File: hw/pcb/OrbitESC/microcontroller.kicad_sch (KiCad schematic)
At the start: 82 parts, among them J2 Micro_SD_Card_Det, J6 CAN1, J7 Serial1, J8 Serial2, J9 CAN2, U1 TLE9250X, U10 TLE9250X, U2 AT25SF081-SSHD-X, U3 24LC128, U4 STM32F446ZCHx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

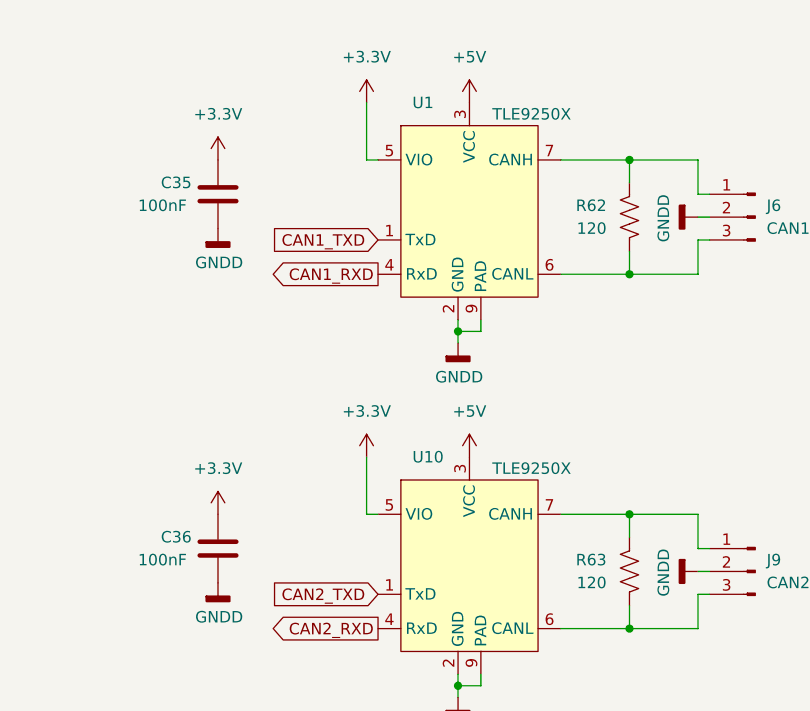
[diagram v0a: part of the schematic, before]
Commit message: Update PCB to match schematic
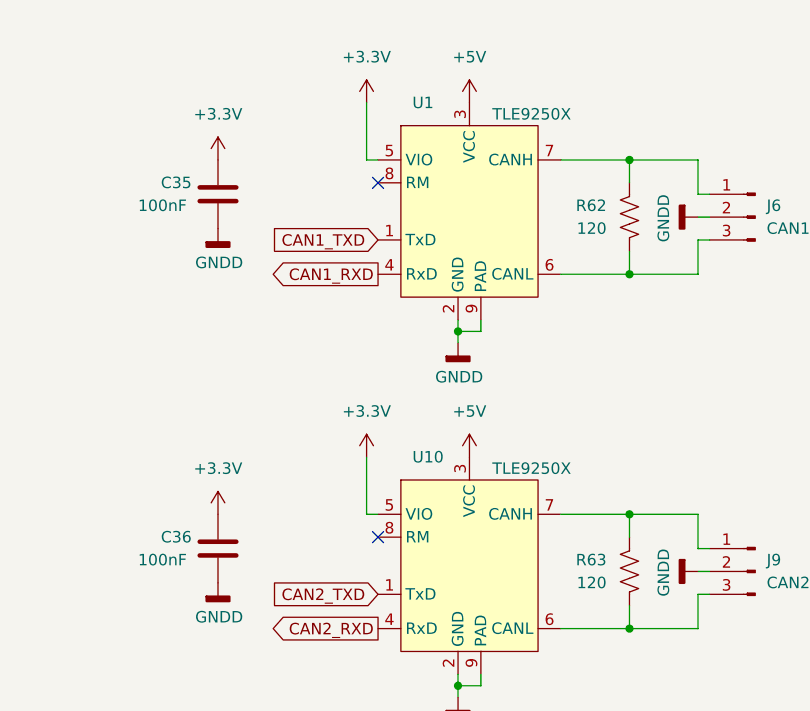
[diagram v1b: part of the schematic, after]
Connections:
- no-connect marks 55 -> 57
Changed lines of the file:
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@@
   (junction (at 212.09 59.69) (diameter 0) (color 0 0 0 0)
   )
+  (no_connect (at 54.61 153.67))
+  (no_connect (at 54.61 193.04))
   (no_connect (at 232.41 124.46))
   (no_connect (at 166.37 114.3))
@@
     (pin "2")
   )
-  (symbol (lib_id "CANTransciever:TLE9250X") (at 64.77 196.85 0) (unit 1)
+  (symbol (lib_name "TLE9250X_1") (lib_id "CANTransciever:TLE9250X") (at 64.77 196.85 0) (unit 1)
     (in_bom yes) (on_board yes)
     (property "Reference" "U10" (id 0) (at 58.42 184.15 0)
@@
     (pin "6")
     (pin "7")
+    (pin "8")
     (pin "9")
   )
@@
       (effects (font (size 1.27 1.27)) hide)
     )
-    (property "Datasheet" "https://www.mouser.com/datasheet/2/590/DS-AT25SF081_045-1385733.pdf" (id 3) (at 337.82 208.28 0)
+    (property "Datasheet" "https://www.adestotech.com/wp-content/uploads/DS-AT25SF081_045.pdf" (id 3) (at 337.82 208.28 0)
       (effects (font (size 1.27 1.27)) hide)
     )
@@
     (pin "6")
     (pin "7")
+    (pin "8")
     (pin "9")
   )

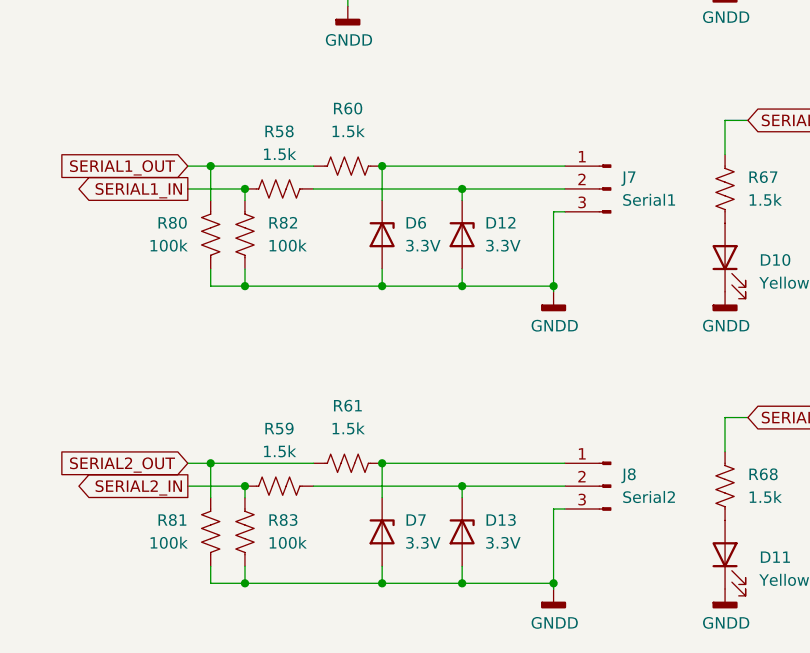
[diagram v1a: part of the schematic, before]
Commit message: Route analogs and power stage sections
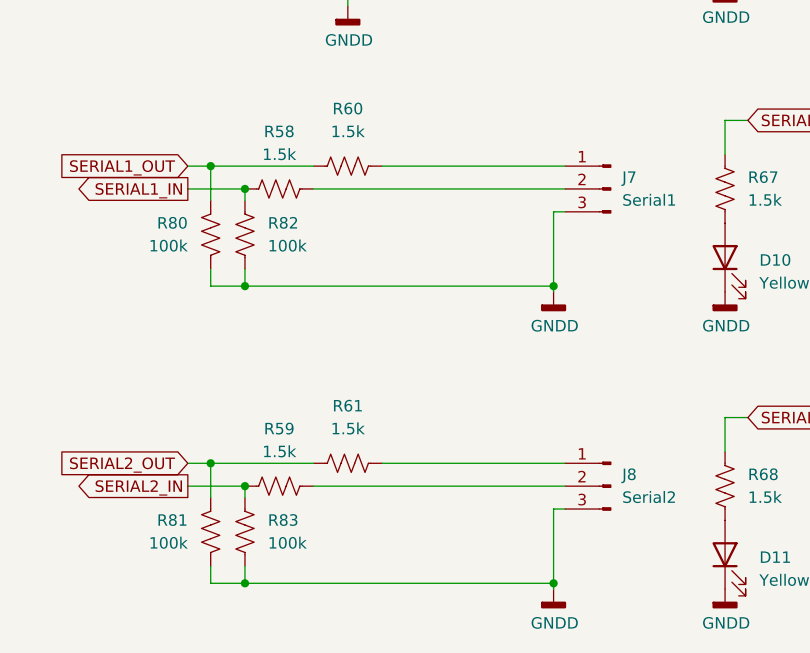
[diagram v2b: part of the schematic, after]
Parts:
- removed D12, D13, D6, D7: 3.3V, Diode_SMD:D_MiniMELF, symbol Device:D_Zener
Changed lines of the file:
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@@
   (junction (at 34.29 27.94) (diameter 0) (color 0 0 0 0)
   )
-  (junction (at 76.2 264.16) (diameter 0) (color 0 0 0 0)
-  )
-  (junction (at 67.31 261.62) (diameter 0) (color 0 0 0 0)
-  )
-  (junction (at 76.2 231.14) (diameter 0) (color 0 0 0 0)
-  )
   (junction (at 196.85 248.92) (diameter 0) (color 0 0 0 0)
   )
@@
   (junction (at 49.53 45.72) (diameter 0) (color 0 0 0 0)
   )
-  (junction (at 67.31 228.6) (diameter 0) (color 0 0 0 0)
-  )
   (junction (at 207.01 59.69) (diameter 0) (color 0 0 0 0)
   )
@@
   (junction (at 304.8 100.33) (diameter 0) (color 0 0 0 0)
   )
-  (junction (at 67.31 241.935) (diameter 0) (color 0 0 0 0)
-  )
   (junction (at 304.8 115.57) (diameter 0) (color 0 0 0 0)
   )
@@
   (junction (at 199.39 248.92) (diameter 0) (color 0 0 0 0)
   )
-  (junction (at 76.2 274.955) (diameter 0) (color 0 0 0 0)
-  )
   (junction (at 82.55 163.83) (diameter 0) (color 0 0 0 0)
   )
@@
   (junction (at 204.47 248.92) (diameter 0) (color 0 0 0 0)
   )
-  (junction (at 76.2 241.935) (diameter 0) (color 0 0 0 0)
-  )
   (junction (at 308.61 210.82) (diameter 0) (color 0 0 0 0)
   )
   (junction (at 321.31 205.74) (diameter 0) (color 0 0 0 0)
   )
-  (junction (at 67.31 274.955) (diameter 0) (color 0 0 0 0)
-  )
   (junction (at 82.55 151.13) (diameter 0) (color 0 0 0 0)
   )
@@
     (stroke (width 0) (type default) (color 0 0 0 0))
   )
-  (wire (pts (xy 76.2 273.05) (xy 76.2 274.955))
-    (stroke (width 0) (type default) (color 0 0 0 0))
-  )
   (wire (pts (xy 322.58 213.36) (xy 308.61 213.36))
     (stroke (width 0) (type default) (color 0 0 0 0))
@@
     (stroke (width 0) (type default) (color 0 0 0 0))
   )
-  (wire (pts (xy 76.2 231.14) (xy 87.63 231.14))
+  (wire (pts (xy 59.69 231.14) (xy 87.63 231.14))
     (stroke (width 0) (type default) (color 0 0 0 0))
   )
@@
     (stroke (width 0) (type default) (color 0 0 0 0))
   )
-  (wire (pts (xy 67.31 240.03) (xy 67.31 241.935))
-    (stroke (width 0) (type default) (color 0 0 0 0))
-  )
   (wire (pts (xy 347.98 175.26) (xy 337.82 175.26))
     (stroke (width 0) (type default) (color 0 0 0 0))
@@
     (stroke (width 0) (type default) (color 0 0 0 0))
   )
-  (wire (pts (xy 76.2 264.16) (xy 87.63 264.16))
-    (stroke (width 0) (type default) (color 0 0 0 0))
-  )
   (wire (pts (xy 204.47 59.69) (xy 204.47 63.5))
     (stroke (width 0) (type default) (color 0 0 0 0))
@@
     (stroke (width 0) (type default) (color 0 0 0 0))
   )
-  (wire (pts (xy 67.31 273.05) (xy 67.31 274.955))
-    (stroke (width 0) (type default) (color 0 0 0 0))
-  )
   (wire (pts (xy 321.31 203.2) (xy 322.58 203.2))
     (stroke (width 0) (type default) (color 0 0 0 0))
@@
     (stroke (width 0) (type default) (color 0 0 0 0))
   )
-  (wire (pts (xy 67.31 274.955) (xy 76.2 274.955))
-    (stroke (width 0) (type default) (color 0 0 0 0))
-  )
   (wire (pts (xy 201.93 248.92) (xy 199.39 248.92))
     (stroke (width 0) (type default) (color 0 0 0 0))
@@
     (stroke (width 0) (type default) (color 0 0 0 0))
   )
-  (wire (pts (xy 76.2 264.16) (xy 76.2 265.43))
-    (stroke (width 0) (type default) (color 0 0 0 0))
-  )
   (wire (pts (xy 309.88 105.41) (xy 346.71 105.41))
     (stroke (width 0) (type default) (color 0 0 0 0))
@@
     (stroke (width 0) (type default) (color 0 0 0 0))
   )
-  (wire (pts (xy 76.2 240.03) (xy 76.2 241.935))
-    (stroke (width 0) (type default) (color 0 0 0 0))
-  )
   (wire (pts (xy 109.22 41.91) (xy 106.68 41.91))
     (stroke (width 0) (type default) (color 0 0 0 0))
@@
     (stroke (width 0) (type default) (color 0 0 0 0))
   )
-  (wire (pts (xy 59.69 264.16) (xy 76.2 264.16))
+  (wire (pts (xy 59.69 264.16) (xy 87.63 264.16))
     (stroke (width 0) (type default) (color 0 0 0 0))
   )
@@
     (stroke (width 0) (type default) (color 0 0 0 0))
   )
-  (wire (pts (xy 76.2 241.935) (xy 86.36 241.935))
+  (wire (pts (xy 52.07 241.935) (xy 86.36 241.935))
     (stroke (width 0) (type default) (color 0 0 0 0))
   )
@@
     (stroke (width 0) (type default) (color 0 0 0 0))
   )
-  (wire (pts (xy 67.31 241.935) (xy 76.2 241.935))
-    (stroke (width 0) (type default) (color 0 0 0 0))
-  )
   (wire (pts (xy 327.66 168.91) (xy 327.66 175.26))
     (stroke (width 0) (type default) (color 0 0 0 0))
@@
     (stroke (width 0) (type default) (color 0 0 0 0))
   )
-  (wire (pts (xy 52.07 274.955) (xy 67.31 274.955))
+  (wire (pts (xy 52.07 274.955) (xy 86.36 274.955))
     (stroke (width 0) (type default) (color 0 0 0 0))
   )
@@
     (stroke (width 0) (type default) (color 0 0 0 0))
   )
-  (wire (pts (xy 59.69 231.14) (xy 76.2 231.14))
-    (stroke (width 0) (type default) (color 0 0 0 0))
-  )
-  (wire (pts (xy 52.07 241.935) (xy 67.31 241.935))
-    (stroke (width 0) (type default) (color 0 0 0 0))
-  )
   (wire (pts (xy 350.52 163.83) (xy 349.25 163.83))
     (stroke (width 0) (type default) (color 0 0 0 0))
@@
     (stroke (width 0) (type default) (color 0 0 0 0))
   )
-  (wire (pts (xy 67.31 261.62) (xy 67.31 265.43))
-    (stroke (width 0) (type default) (color 0 0 0 0))
-  )
   (wire (pts (xy 330.2 87.63) (xy 330.2 85.09))
     (stroke (width 0) (type default) (color 0 0 0 0))
@@
     (stroke (width 0) (type default) (color 0 0 0 0))
   )
-  (wire (pts (xy 76.2 231.14) (xy 76.2 232.41))
-    (stroke (width 0) (type default) (color 0 0 0 0))
-  )
   (wire (pts (xy 52.07 115.57) (xy 54.61 115.57))
     (stroke (width 0) (type default) (color 0 0 0 0))
@@
     (stroke (width 0) (type default) (color 0 0 0 0))
   )
-  (wire (pts (xy 67.31 228.6) (xy 67.31 232.41))
-    (stroke (width 0) (type default) (color 0 0 0 0))
-  )
-  (wire (pts (xy 76.2 274.955) (xy 86.36 274.955))
-    (stroke (width 0) (type default) (color 0 0 0 0))
-  )
   (wire (pts (xy 194.31 248.92) (xy 194.31 251.46))
     (stroke (width 0) (type default) (color 0 0 0 0))
@@
     (pin "1")
   )
-  (symbol (lib_id "Device:D_Zener") (at 76.2 236.22 270) (unit 1)
-    (in_bom yes) (on_board yes) (fields_autoplaced)
-    (property "Reference" "D12" (id 0) (at 78.74 234.9499 90)
-      (effects (font (size 1.27 1.27)) (justify left))
-    )
-    (property "Value" "3.3V" (id 1) (at 78.74 237.4899 90)
-      (effects (font (size 1.27 1.27)) (justify left))
-    )
-    (property "Footprint" "Diode_SMD:D_MiniMELF" (id 2) (at 76.2 236.22 0)
-      (effects (font (size 1.27 1.27)) hide)
-    )
-    (property "Datasheet" "~" (id 3) (at 76.2 236.22 0)
-      (effects (font (size 1.27 1.27)) hide)
-    )
-    (property "JLCPCB" "C8056" (id 4) (at 76.2 236.22 90)
-      (effects (font (size 1.27 1.27)) hide)
-    )
-    (pin "1")
-    (pin "2")
-  )
   (symbol (lib_id "power:GNDD") (at 294.64 57.15 0) (unit 1)
     (in_bom yes) (on_board yes)
@@
     (pin "2")
   )
-  (symbol (lib_id "Device:D_Zener") (at 67.31 269.24 270) (unit 1)
-    (in_bom yes) (on_board yes) (fields_autoplaced)
-    (property "Reference" "D7" (id 0) (at 69.85 267.9699 90)
-      (effects (font (size 1.27 1.27)) (justify left))
-    )
-    (property "Value" "3.3V" (id 1) (at 69.85 270.5099 90)
-      (effects (font (size 1.27 1.27)) (justify left))
-    )
-    (property "Footprint" "Diode_SMD:D_MiniMELF" (id 2) (at 67.31 269.24 0)
-      (effects (font (size 1.27 1.27)) hide)
-    )
-    (property "Datasheet" "~" (id 3) (at 67.31 269.24 0)
-      (effects (font (size 1.27 1.27)) hide)
-    )
-    (property "JLCPCB" "C8056" (id 4) (at 67.31 269.24 90)
-      (effects (font (size 1.27 1.27)) hide)
-    )
-    (pin "1")
-    (pin "2")
-  )
   (symbol (lib_id "Device:LED") (at 105.41 238.76 90) (unit 1)
     (in_bom yes) (on_board yes) (fields_autoplaced)
@@
     (pin "2")
   )
-  (symbol (lib_id "Device:D_Zener") (at 76.2 269.24 270) (unit 1)
-    (in_bom yes) (on_board yes) (fields_autoplaced)
-    (property "Reference" "D13" (id 0) (at 78.74 267.9699 90)
-      (effects (font (size 1.27 1.27)) (justify left))
-    )
-    (property "Value" "3.3V" (id 1) (at 78.74 270.5099 90)
-      (effects (font (size 1.27 1.27)) (justify left))
-    )
-    (property "Footprint" "Diode_SMD:D_MiniMELF" (id 2) (at 76.2 269.24 0)
-      (effects (font (size 1.27 1.27)) hide)
-    )
-    (property "Datasheet" "~" (id 3) (at 76.2 269.24 0)
-      (effects (font (size 1.27 1.27)) hide)
-    )
-    (property "JLCPCB" "C8056" (id 4) (at 76.2 269.24 90)
-      (effects (font (size 1.27 1.27)) hide)
-    )
-    (pin "1")
-    (pin "2")
-  )
   (symbol (lib_id "Device:C") (at 36.83 194.31 180) (unit 1)
     (in_bom yes) (on_board yes)
@@
       (effects (font (size 1.27 1.27)) hide)
     )
-    (pin "1")
-    (pin "2")
-  )
-  (symbol (lib_id "Device:D_Zener") (at 67.31 236.22 270) (unit 1)
-    (in_bom yes) (on_board yes) (fields_autoplaced)
-    (property "Reference" "D6" (id 0) (at 69.85 234.9499 90)
-      (effects (font (size 1.27 1.27)) (justify left))
-    )
-    (property "Value" "3.3V" (id 1) (at 69.85 237.4899 90)
-      (effects (font (size 1.27 1.27)) (justify left))
-    )
-    (property "Footprint" "Diode_SMD:D_MiniMELF" (id 2) (at 67.31 236.22 0)
-      (effects (font (size 1.27 1.27)) hide)
-    )
-    (property "Datasheet" "~" (id 3) (at 67.31 236.22 0)
-      (effects (font (size 1.27 1.27)) hide)
-    )
-    (property "JLCPCB" "C8056" (id 4) (at 67.31 236.22 90)
-      (effects (font (size 1.27 1.27)) hide)
-    )

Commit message: Start rework of processor selection after realizing I can't afford manufacturing...
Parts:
- removed C33: 2.2uF, Capacitor_SMD:C_0805_2012Metric, symbol Device:C
- removed C34, C36, C49, C56: 100nF, Capacitor_SMD:C_0402_1005Metric, symbol Device:C
- removed D11, D9: Yellow LED, Diode_SMD:D_0603_1608Metric, symbol Device:LED
- removed J2: Micro_SD_Card_Det, Connector_Card:microSD_HC_Molex_104031-0811, symbol Connector:Micro_SD_Card_Det
- removed J8: Serial2, Connector_JST:JST_PH_B3B-PH-K_1x03_P2.00mm_Vertical, symbol Connector:Conn_01x03_Male
- removed J9: CAN2, Connector_JST:JST_PH_B3B-PH-K_1x03_P2.00mm_Vertical, symbol Connector:Conn_01x03_Male
- removed R59, R61, R66, R68: 1.5k, Resistor_SMD:R_0402_1005Metric, symbol Device:R_US
- removed R63: 120, Resistor_SMD:R_0402_1005Metric, symbol Device:R_US
- removed R71: 10k, Resistor_SMD:R_0402_1005Metric, symbol Device:R_US
- removed R72, R73, R74, R75, R76: 39k, Resistor_SMD:R_0402_1005Metric, symbol Device:R_US
- removed R81, R83: 100k, Resistor_SMD:R_0402_1005Metric, symbol Device:R_US
- removed TP1: SDIO_CMD, TestPoint:TestPoint_Pad_D1.0mm, symbol Connector:TestPoint_Small
- removed TP2: SDIO_DATA_2, TestPoint:TestPoint_Pad_D1.0mm, symbol Connector:TestPoint_Small
- removed TP3: SDIO_DATA_0, TestPoint:TestPoint_Pad_D1.0mm, symbol Connector:TestPoint_Small
- removed TP4: SDIO_CARD_DETECT, TestPoint:TestPoint_Pad_D1.0mm, symbol Connector:TestPoint_Small
- removed TP6: SDIO_DATA_3, TestPoint:TestPoint_Pad_D1.0mm, symbol Connector:TestPoint_Small
- removed TP7: SDIO_CLK, TestPoint:TestPoint_Pad_D1.0mm, symbol Connector:TestPoint_Small
- removed TP8: SDIO_DATA_1, TestPoint:TestPoint_Pad_D1.0mm, symbol Connector:TestPoint_Small
- removed U10: TLE9250X, Package_SON:HVSON-8-1EP_3x3mm_P0.65mm_EP1.6x2.4mm, symbol CANTransciever:TLE9250X
- removed U4: STM32F446ZCHx, Package_BGA:UFBGA-144_7x7mm_Layout12x12_P0.5mm, symbol MCU_ST_STM32F4:STM32F446ZCHx
- removed X1: ECS-2520MV-240-BN, Oscillator:Oscillator_SMD_ECS_2520MV-xxx-xx-4Pin_2.5x2.0mm, symbol Oscillator:ECS-2520MV-xxx-xx
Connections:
- net JTAG_TCLK: no longer names the net of J10.4 (Pin_4)
- net JTAG_TDI: no longer names the net of J10.8 (Pin_8)
- net JTAG_TDO: no longer names the net of J10.6 (Pin_6)
- net JTAG_TMS: no longer names the net of J10.2 (Pin_2)
- no-connect marks 57 -> 2
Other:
- removed sheet USBCircuitry
- sheet InputButton ports: added none; removed BOOT1, BREAK, USER
- note added: "Add USB to serial converter from Luminary and remove serial header"
- note removed: "24MHz Oscillator"
- moved on the sheet: D10, J7, R58, R60, R67, R80, R82
